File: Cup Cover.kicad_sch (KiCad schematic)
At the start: 7 parts, among them SW1 SW_Push, SW2 SW_Reed

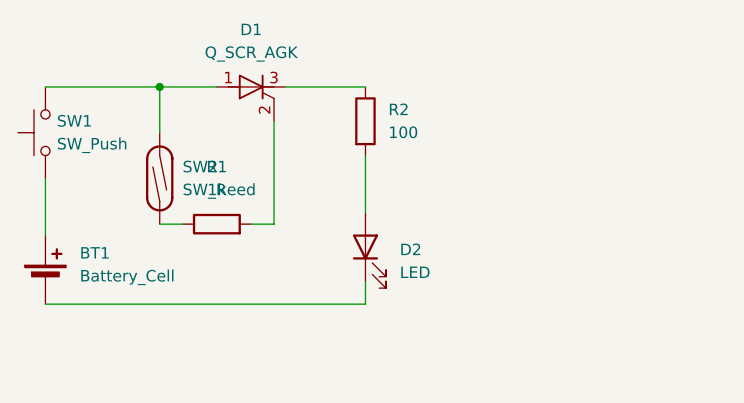
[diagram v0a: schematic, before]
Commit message: board review 1 (battery footp, reed sw)
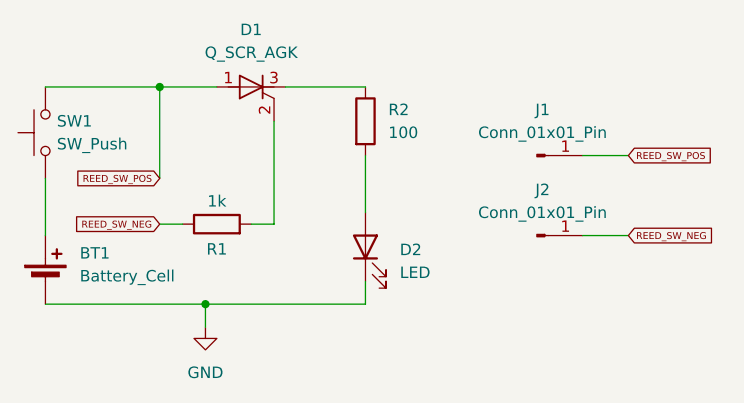
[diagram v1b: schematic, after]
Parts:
- removed SW2: SW_Reed, Button_Switch_SMD:SW_SPST_REED_CT05-XXXX-G1, symbol Switch:SW_Reed
- added J1, J2: Conn_01x01_Pin, PH1-01-UA:ADAM-TECH_PH1-01-UA, symbol Connector:Conn_01x01_Pin
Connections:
- net REED_SW_POS: now reaches D1.1 (A), SW1.2
- net REED_SW_POS: now also J1.1 (Pin_1)
- net GND: now reaches BT1.N (-), D2.1 (K)
- net REED_SW_NEG: now reaches R1.1
- net REED_SW_NEG: now also J2.1 (Pin_1)
